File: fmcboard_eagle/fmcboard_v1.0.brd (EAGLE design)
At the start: 98 x 74 mm, 50 parts, among them IC1 OPA699ID, IC2 OPA699ID, IC3 ICL7660CPA, IC4 ICL7660CPA, J1 8pin, J12 4p-2.54, J2 ASP-134604-01, J3 4p-2.54, J4 4p-2.54, J5 8pin, U1 TXS0108EPWR

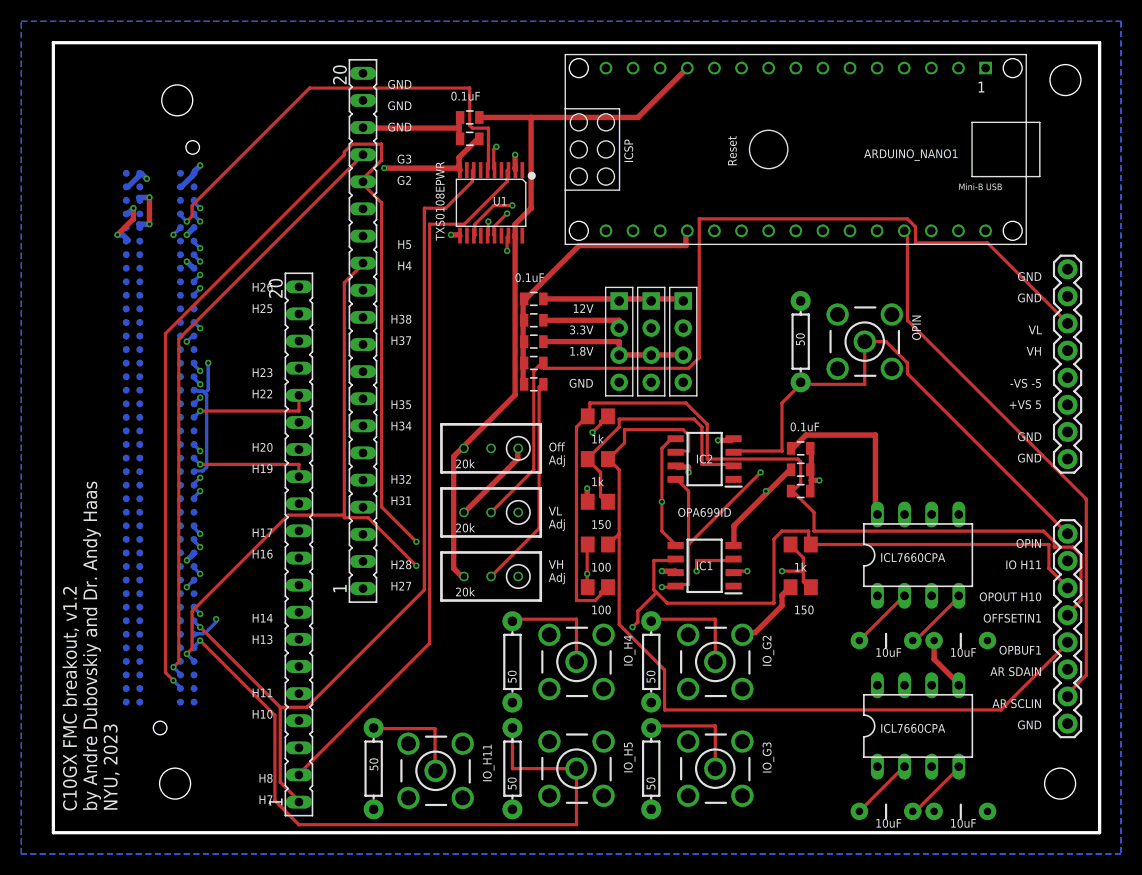
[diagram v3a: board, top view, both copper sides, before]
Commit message: add lm358 op amp buffer for offset
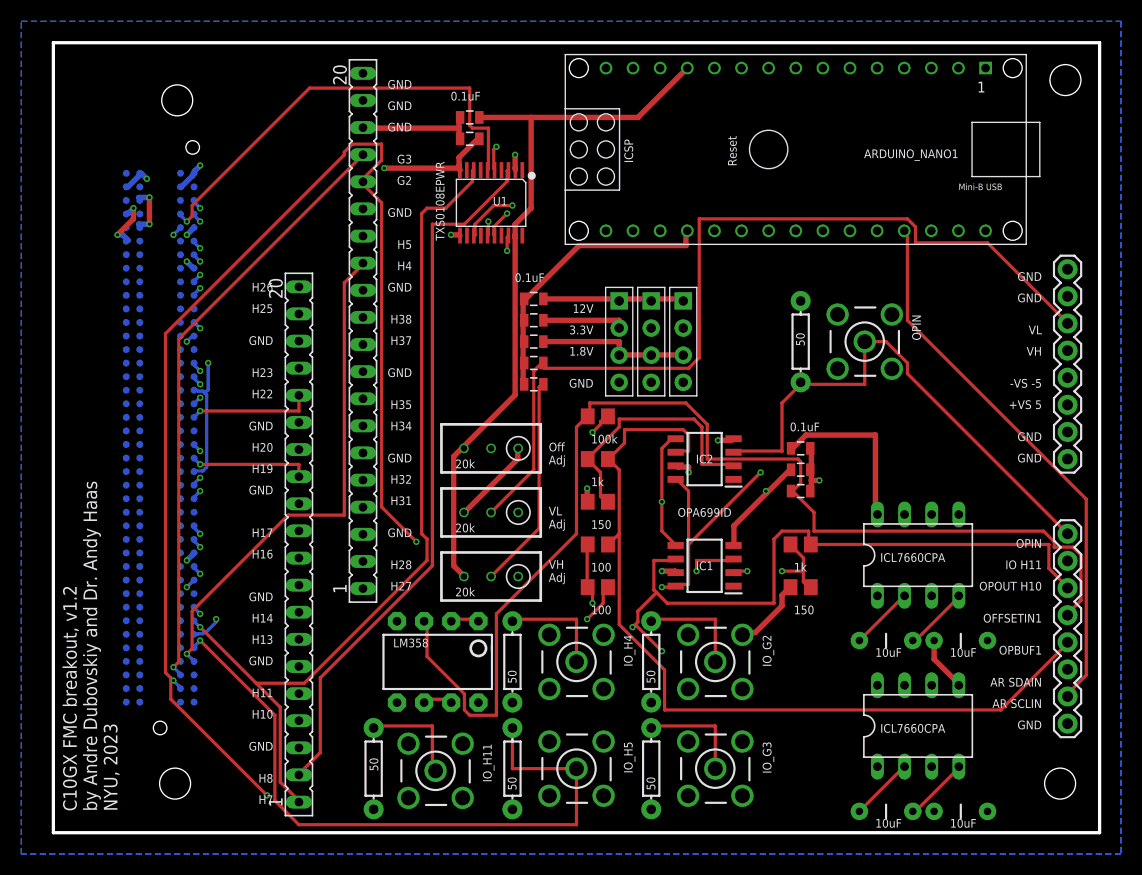
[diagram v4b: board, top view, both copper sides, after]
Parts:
- added IC5: LM358, SparkFun-AnalogIC:DIP08
- R3: value 1k -> 100k
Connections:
- removed net +VS: ARDUINO_NANO1.12, C3.1, C9.1, IC1.7, IC2.7, IC3.8, IC4.8, J1.3, R1.3, R7.3, U1.19
- removed net -VS: C10.1, C2.1, C6.1, IC1.4, IC2.4, IC3.5, IC4.5, J1.4, R1.1, R8.3
- new net N$9: IC5.6, IC5.7
- new net VIN1: IC5.1, IC5.2, R14.2
- new net VS+: ARDUINO_NANO1.12, C3.1, C9.1, IC1.7, IC2.7, IC3.8, IC4.8, IC5.8, J1.3, R1.3, R7.3, U1.19
- new net VS-: C10.1, C2.1, C6.1, IC1.4, IC2.4, IC3.5, IC4.5, IC5.4, J1.4, R1.1, R8.3
- net GND: now also IC5.5, SV1.12, SV1.15, SV1.18, SV1.3, SV1.6, SV1.9, SV2.12, SV2.15, SV2.3, SV2.6, SV2.9
- net OFFSETIN1: now also IC5.3; no longer R14.2
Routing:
- net VS+: track 0.00 -> 189.8 mm, vias 0 -> 2
- net +VS: track 177.5 -> 0.00 mm, vias 2 -> 0
- net VS-: track 0.00 -> 143.8 mm, vias 0 -> 2
- net -VS: track 130.9 -> 0.00 mm, vias 2 -> 0
- net G2: track 137.0 -> 177.4 mm, vias 2 -> 3
- net OFFSETIN1: track 86.9 -> 110.2 mm
- net H4: track 77.8 -> 97.3 mm, vias 2 -> 1
- net VIN1: track 0.00 -> 18.1 mm, vias 0 -> 1
- net IO2_H11: track 101.8 -> 110.2 mm
- net H5: track 114.9 -> 121.9 mm
- net OPOUT1_H10: track 123.5 -> 130.3 mm, vias 2 -> 3
- net N$9: track 0.00 -> 2.82 mm
- net N$1: track 19.4 -> 21.5 mm

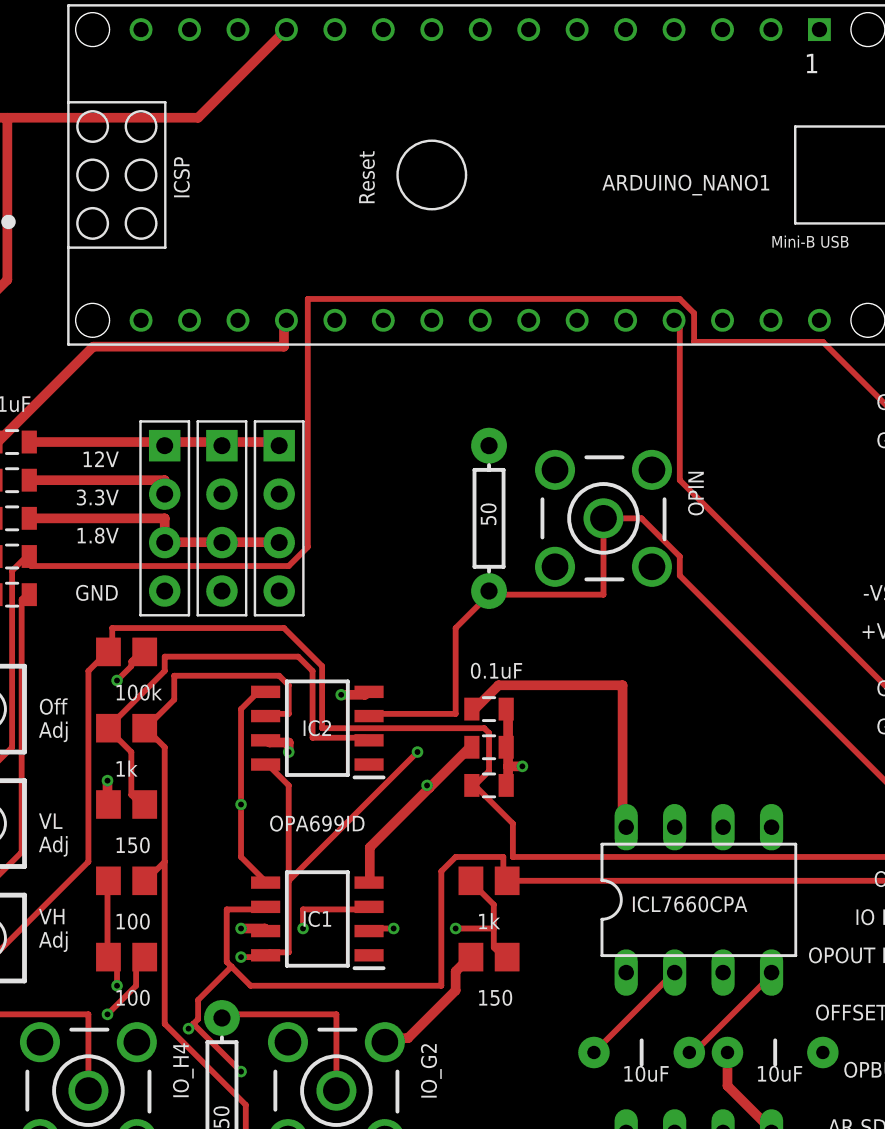
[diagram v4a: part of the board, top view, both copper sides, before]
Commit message: Update gain resistor values
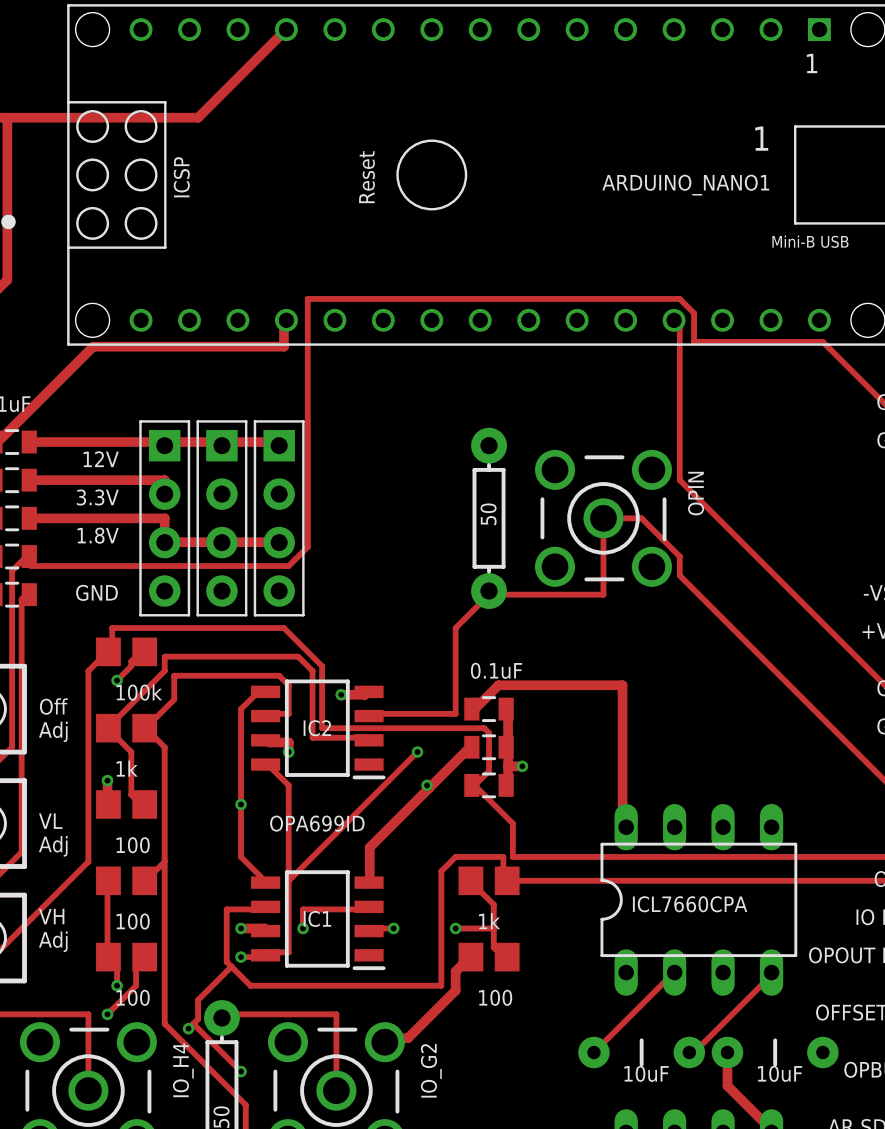
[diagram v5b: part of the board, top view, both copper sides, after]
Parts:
- ARDUINO_NANO1: value (none) -> 1
- R10, R12: value 150 -> 100
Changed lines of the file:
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@@
 <drawing>
 <settings>
-<setting alwaysvectorfont="yes"/>
+<setting alwaysvectorfont="no"/>
 <setting verticaltext="up"/>
 </settings>
@@
 <attribute name="VALUE" x="39.5" y="28.95" size="0.8128" layer="21" rot="R180"/>
 </element>
-<element name="ARDUINO_NANO1" library="ArduinoNanoV30" package="ARDUINO_NANO" value="" x="67" y="64" smashed="yes" rot="R180">
+<element name="ARDUINO_NANO1" library="ArduinoNanoV30" package="ARDUINO_NANO" value="1" x="67" y="64" smashed="yes" rot="R180">
 <attribute name="NAME" x="84.78" y="64" size="0.8128" layer="21" rot="R180"/>
 <attribute name="VALUE" x="84.78" y="66.54" size="1.27" layer="21" font="vector" rot="R180"/>
@@
 <attribute name="VALUE" x="69.365" y="24.46" size="0.8128" layer="21"/>
 </element>
-<element name="R10" library="rcl" library_urn="urn:adsk.eagle:library:334" package="R0805" package3d_urn="urn:adsk.eagle:package:23553/2" value="150" x="70" y="23" smashed="yes">
+<element name="R10" library="rcl" library_urn="urn:adsk.eagle:library:334" package="R0805" package3d_urn="urn:adsk.eagle:package:23553/2" value="100" x="70" y="23" smashed="yes">
 <attribute name="POPULARITY" value="85" x="70" y="23" size="1.778" layer="27" display="off"/>
 <attribute name="SPICEPREFIX" value="R" x="70" y="23" size="1.778" layer="27" display="off"/>
@@
 <attribute name="VALUE" x="50.365" y="32.46" size="0.8128" layer="21"/>
 </element>
-<element name="R12" library="rcl" library_urn="urn:adsk.eagle:library:334" package="R0805" package3d_urn="urn:adsk.eagle:package:23553/2" value="150" x="51" y="31" smashed="yes">
+<element name="R12" library="rcl" library_urn="urn:adsk.eagle:library:334" package="R0805" package3d_urn="urn:adsk.eagle:package:23553/2" value="100" x="51" y="31" smashed="yes">
 <attribute name="POPULARITY" value="85" x="51" y="31" size="1.778" layer="27" display="off"/>
 <attribute name="SPICEPREFIX" value="R" x="51" y="31" size="1.778" layer="27" display="off"/>

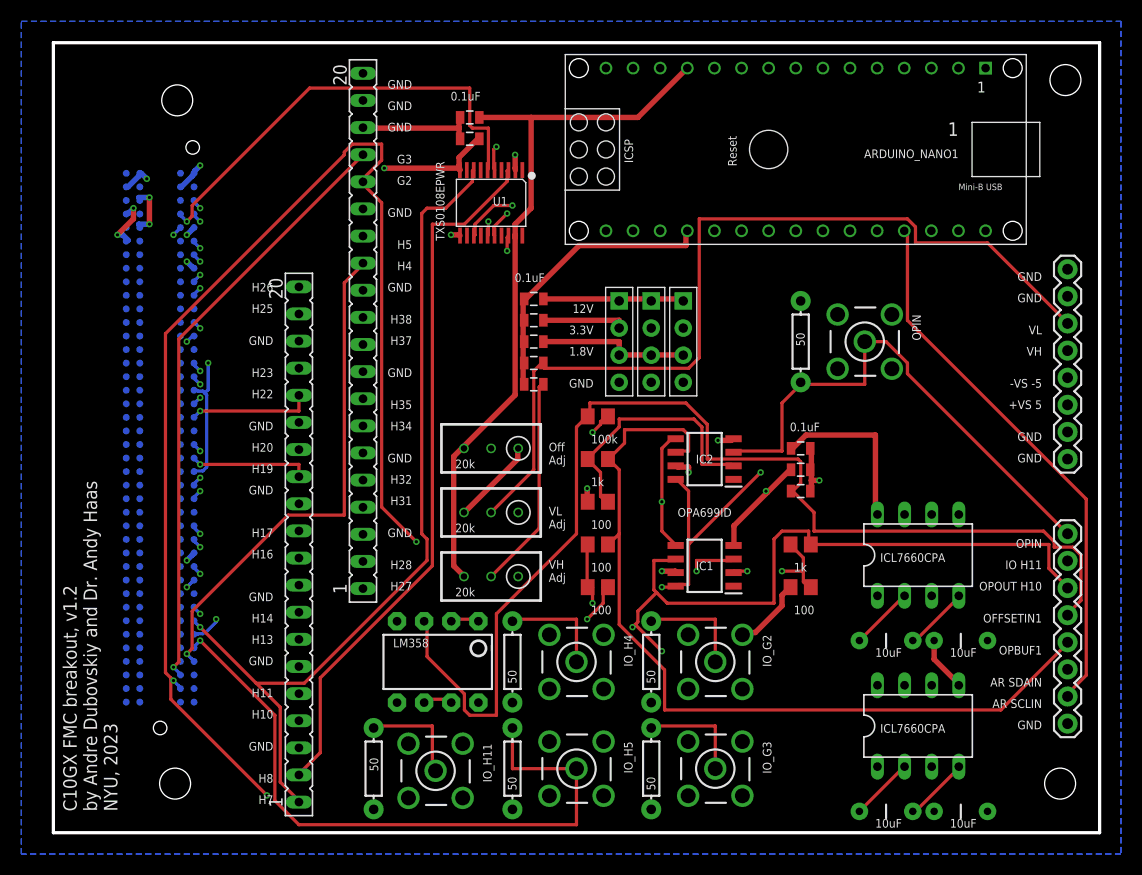
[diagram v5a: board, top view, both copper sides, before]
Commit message: use bss138 level shifting
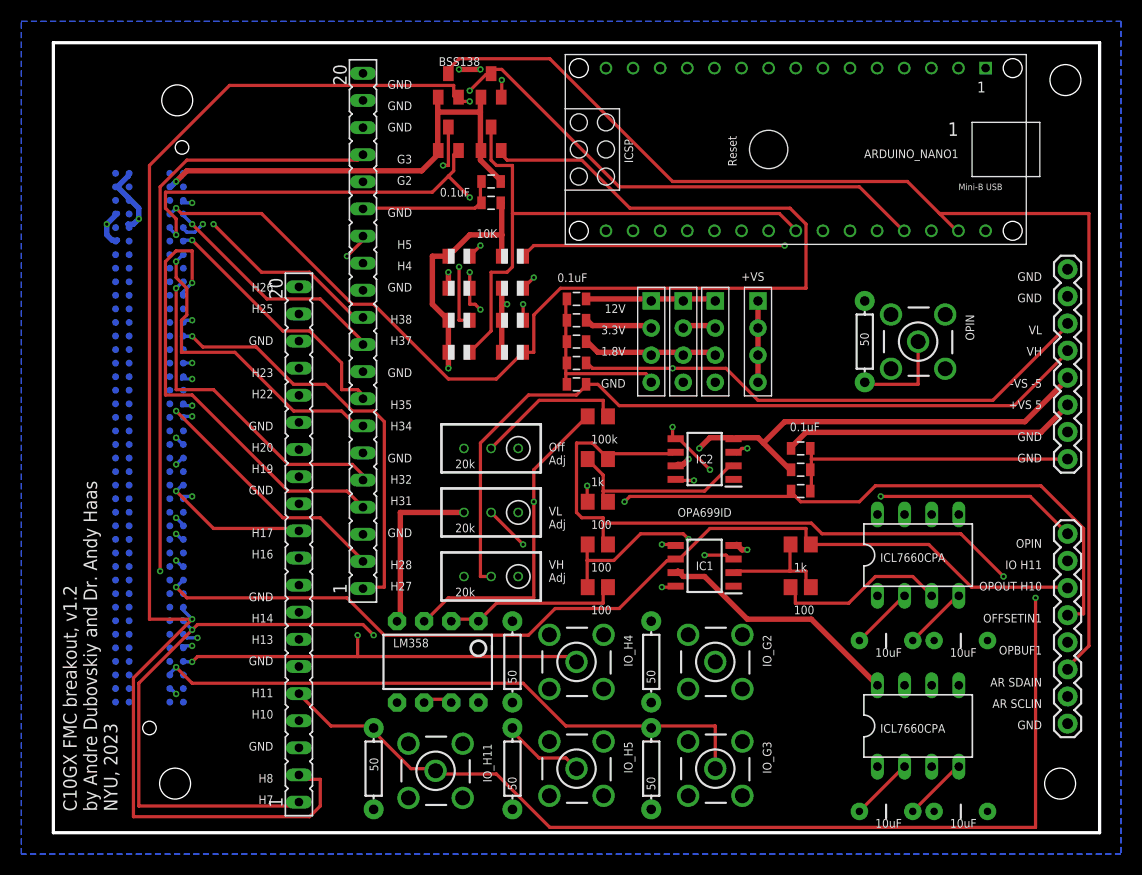
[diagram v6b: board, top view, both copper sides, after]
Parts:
- removed U1: TXS0108EPWR, Seeed-IC:TSSOP20-0.65-6.5X4.4MM
- added J6: 4p-2.54, Seeed-Connector:H4-2.54
- added Q1, Q2, Q3, Q4: BSS138, adafruit:SOT23
- added R17, R18, R19, R20, R21, R22, R23, R24: 10K, adafruit:R0805
- moved C9 8.25 mm to (41.0, 59.0)
- moved R2 6.00 mm to (76.0, 46.0)
- moved OPIN 5.00 mm to (81.0, 46.0)
- moved C14 4.47 mm to (41.0, 61.0)
- moved C12 4.00 mm to (49.0, 50.0)
- moved C13 4.00 mm to (49.0, 48.0)
- moved C5 4.00 mm to (49.0, 46.0)
- moved C7 4.00 mm to (49.0, 42.0)
- moved C8 4.00 mm to (49.0, 44.0)
- moved J12 3.00 mm to (56.0, 46.0)
- moved J3 3.00 mm to (62.0, 46.0)
- moved J4 3.00 mm to (59.0, 46.0)
- moved J2 1.00 mm to (9.00, 37.0)
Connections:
- net 1V8: now also Q1.1, Q2.1, Q3.1, Q4.1, R18.1, R20.1, R22.1, R24.1; no longer U1.10, U1.2
- net AR_G36: now also Q3.3, R21.2; no longer U1.16
- net AR_G37: now also Q4.3, R23.2; no longer U1.15
- net AR_SCLIN: now also Q1.3, R19.2; no longer U1.13
- net AR_SDAIN: now also Q2.3, R17.2; no longer U1.18
- net G36: now also Q3.2, R22.2; no longer U1.5
- net G37: now also Q4.2, R24.2; no longer U1.6
- net GND: no longer U1.11
- net SCLIN: now also Q1.2, R20.2; no longer U1.8
- net SDAIN: now also Q2.2, R18.2; no longer U1.3
- net VS+: now also J6.1, J6.2, J6.3, J6.4, R17.1, R19.1, R21.1, R23.1; no longer U1.19
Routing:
- net G37: track 42.5 -> 109.6 mm
- net SDAIN: track 87.6 -> 146.6 mm, vias 1 -> 3
- net AR_SDAIN: track 97.1 -> 154.6 mm
- net VS+: track 189.8 -> 235.2 mm
- net AR_G36: track 33.1 -> 73.2 mm, vias 1 -> 2
- net G2: track 177.4 -> 141.5 mm, vias 3 -> 1
- net H5: track 121.9 -> 87.3 mm, vias 1 -> 2
- net SCLIN: track 81.7 -> 115.9 mm, vias 1 -> 5
- net AR_SCLIN: track 94.4 -> 126.4 mm, vias 1 -> 2
- net GND: track 105.7 -> 80.7 mm, vias 8 -> 3
- net 1V8: track 96.1 -> 118.3 mm
- net AR_G37: track 31.0 -> 52.6 mm, vias 1 -> 0
- net VL: track 111.9 -> 90.9 mm, vias 1 -> 5
- net VS-: track 143.8 -> 163.8 mm
- net 12V: track 69.0 -> 88.6 mm, vias 2 -> 3
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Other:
- board text added: "+VS"

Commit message: switch to C26 and C27
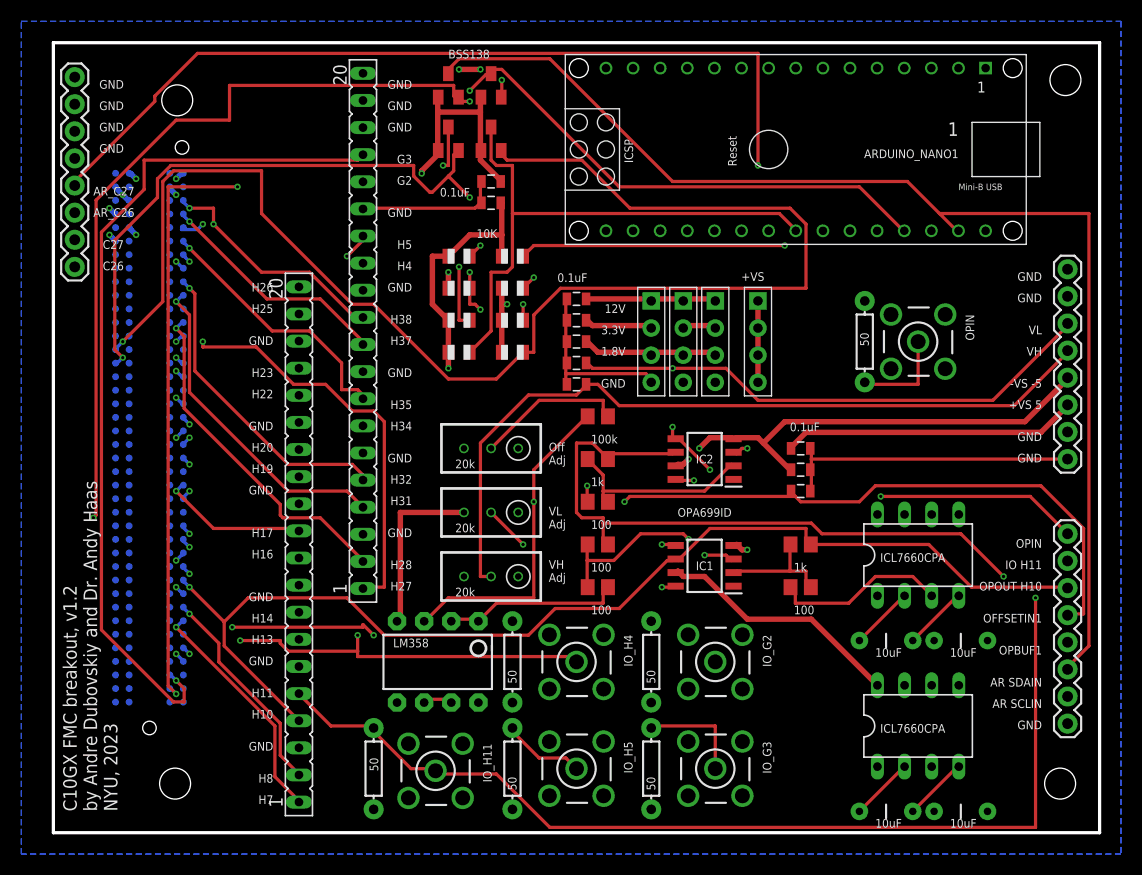
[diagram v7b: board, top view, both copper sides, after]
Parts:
- added J7: 8pin, SparkFun-Connectors:1X08
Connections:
- removed net AR_G36: ARDUINO_NANO1.24, Q3.3, R21.2
- removed net AR_G37: ARDUINO_NANO1.23, Q4.3, R23.2
- removed net G36: J2.G36, Q3.2, R22.2
- removed net G37: J2.G37, Q4.2, R24.2
- new net AR_C26: ARDUINO_NANO1.24, J7.3, Q3.3, R21.2
- new net AR_C27: ARDUINO_NANO1.23, J7.4, Q4.3, R23.2
- new net C26: J2.C26, J7.1, Q3.2, R22.2
- new net C27: J2.C27, J7.2, Q4.2, R24.2
- net GND: now also J7.5, J7.6, J7.7, J7.8
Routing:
- net C27: track 0.00 -> 143.2 mm, vias 0 -> 1
- net AR_C27: track 0.00 -> 140.3 mm, vias 0 -> 1
- net AR_C26: track 0.00 -> 119.2 mm, vias 0 -> 2
- net G37: track 109.6 -> 0.00 mm, vias 1 -> 0
- net C26: track 0.00 -> 79.2 mm, vias 0 -> 3
- net AR_G36: track 73.2 -> 0.00 mm, vias 2 -> 0
- net AR_G37: track 52.6 -> 0.00 mm
- net G36: track 51.7 -> 0.00 mm, vias 3 -> 0
- net G3: track 123.8 -> 147.2 mm, vias 2 -> 1
- net SDAIN: track 146.6 -> 125.9 mm, vias 3 -> 4
- net 1V8: track 118.3 -> 101.1 mm, vias 3 -> 5
- net H31: track 42.9 -> 30.6 mm
- net SCLIN: track 115.9 -> 103.9 mm, vias 5 -> 6
- net OPOUT1_H10: track 114.3 -> 106.5 mm
- net H34: track 30.1 -> 35.1 mm
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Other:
- board text added: "AR_C26"
- board text added: "AR_C27"
- board text added: "C26"
- board text added: "C27"
